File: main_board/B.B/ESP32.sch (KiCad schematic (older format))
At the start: 36 parts

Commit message: konzultace_s_Kubou_01
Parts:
- removed C?: 1nf, symbol Device:C
- removed R?: 1K, Resistor_SMD:R_0402_1005Metric, symbol Device:R
- removed R? (x2): 182, Resistor_SMD:R_0402_1005Metric, symbol Device:R
- added C?: 100nf, symbol Device:C
- added LED? (x2): LED, LED_SMD:LED_0603_1608Metric, symbol B.B-eagle-import:LED
- added R? (x4): 220, symbol Device:R
- added R?: 5k1, Resistor_SMD:R_0402_1005Metric, symbol Device:R
- C?: value 1nf -> 100nf; LCSC C1523 -> C14663
- R?: value 1K -> 5k1; LCSC (none) -> C25905
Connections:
- wire segments 104 -> 109
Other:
- moved on the sheet: C?, Q?, R?

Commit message: preparation_to_drawing_PCB
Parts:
- removed C?: 100nf, symbol Device:C
- removed C?: 1nf, symbol Device:C
- removed Q?: Q_NPN_BCE, symbol Device:Q_NPN_BCE
- removed SW?: SW_DIP_x01, symbol Switch:SW_DIP_x01
- added C?: 100nf, Capacitor_SMD:C_0402_1005Metric, symbol Device:C
- added Q?: Q_NPN_BCE, Package_TO_SOT_SMD:SOT-23, symbol Device:Q_NPN_BCE
- added SW?: SW_DIP_x01, Button_Switch_SMD:SW_Push_1P1T_NO_CK_KSC6xxJ, symbol Switch:SW_DIP_x01
- C?: footprint (none) -> Capacitor_SMD:C_0402_1005Metric; LCSC C14663 -> C1525
- J?: footprint (none) -> Connector_USB:USB_C_Receptacle_Amphenol_12401610E4-2A
- Q?: poznamka nutno vyměnit (musí být -> Vgs-min>1.6V) -> (none)
- Q?: footprint (none) -> Package_TO_SOT_SMD:SOT-23; LCSC (none) -> C125315
- R?: LCSC (none) -> C11702
- SW?: footprint (none) -> Button_Switch_SMD:SW_Push_1P1T_NO_CK_KSC6xxJ
- U?: LCSC (none) -> C105167
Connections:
- net labels added: 5V_USB
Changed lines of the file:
@@
 F 0 "J?" H 2257 3417 50  0000 C CNN
 F 1 "USB_C_Receptacle_USB2.0" H 2257 3326 50  0000 C CNN
-F 2 "" H 2300 2550 50  0001 C CNN
+F 2 "Connector_USB:USB_C_Receptacle_Amphenol_12401610E4-2A" H 2300 2550 50  0001 C CNN
 F 3 "https://www.usb.org/sites/default/files/documents/usb_type-c.zip" H 2300 2550 50  0001 C CNN
 	1    2150 2550
@@
 F 3 "https://datasheet.lcsc.com/szlcsc/Changjiang-Electronics-Tech-CJ-CJ3134K_C110100.pdf" H 3250 1350 50  0001 L CNN
 F 4 "C110100" H 3250 1350 50  0001 C CNN "LCSC"
-F 5 "nutno vyměnit (musí být ->  Vgs-min>1.6V)" H 3250 1350 50  0001 C CNN "poznamka"
 	1    3250 1350
 	0    -1   -1   0
@@
 	3300 2150 2750 2150
 Wire Wire Line
-	2750 1950 3250 1950
+	2750 1950 3050 1950
 Connection ~ 3600 1950
 $Comp
@@
 F 0 "SW?" H 9550 1667 50  0000 C CNN
 F 1 "SW_DIP_x01" H 9550 1576 50  0000 C CNN
-F 2 "" H 9550 1400 50  0001 C CNN
+F 2 "Button_Switch_SMD:SW_Push_1P1T_NO_CK_KSC6xxJ" H 9550 1400 50  0001 C CNN
 F 3 "~" H 9550 1400 50  0001 C CNN
 	1    9550 1400
@@
 Connection ~ 9900 1400
 $Comp
-L Switch:SW_DIP_x01 SW?
-U 1 1 5F936AB7
-P 9550 2400
-F 0 "SW?" H 9550 2667 50  0000 C CNN
-F 1 "SW_DIP_x01" H 9550 2576 50  0000 C CNN
-F 2 "" H 9550 2400 50  0001 C CNN
-F 3 "~" H 9550 2400 50  0001 C CNN
-	1    9550 2400
-	1    0    0    -1
-$EndComp
-$Comp
-L Device:C C?
-U 1 1 5F936ABE
-P 9550 2650
-F 0 "C?" V 9600 2750 50  0000 C CNN
-F 1 "100nf" V 9600 2500 50  0000 C CNN
-F 2 "" H 9588 2500 50  0001 C CNN
-F 3 "~" H 9550 2650 50  0001 C CNN
-F 4 "C14663" V 9550 2650 50  0001 C CNN "LCSC"
-	1    9550 2650
-	0    -1   -1   0
-$EndComp
-$Comp
 L Device:R R?
 U 1 1 5F936AC5
@@
 Connection ~ 9900 2400
 Wire Wire Line
-	10250 2400 10300 2400
-Wire Wire Line
 	10250 1400 10400 1400
 Text Label 10400 1400 0    50   ~ 0
@@
 Text Label 10400 2400 0    50   ~ 0
 EN
-$Comp
-L Device:C C?
-U 1 1 5F943646
-P 10300 2650
-F 0 "C?" V 10350 2750 50  0000 C CNN
-F 1 "1nf" V 10350 2550 50  0000 C CNN
-F 2 "" H 10338 2500 50  0001 C CNN
-F 3 "~" H 10300 2650 50  0001 C CNN
-F 4 "C1523" V 10300 2650 50  0001 C CNN "LCSC"
-	1    10300 2650
-	1    0    0    -1
-$EndComp
-Wire Wire Line
-	10300 2500 10300 2400
-$Comp
-L B.B-eagle-import:GND #GND?
-U 1 1 5F95FE63
-P 10300 2900
-F 0 "#GND?" H 10300 2900 50  0001 C CNN
-F 1 "GND" H 10300 2779 59  0000 C CNN
-F 2 "" H 10300 2900 50  0001 C CNN
-F 3 "" H 10300 2900 50  0001 C CNN
-	1    10300 2900
-	1    0    0    -1
-$EndComp
 Wire Wire Line
 	3600 1950 3900 1950
@@
 F 2 "Package_DFN_QFN:QFN-28-1EP_5x5mm_P0.5mm_EP3.35x3.35mm" H 5750 1450 50  0001 L CNN
 F 3 "https://www.silabs.com/documents/public/data-sheets/cp2102n-datasheet.pdf" H 5350 1900 50  0001 C CNN
+F 4 "C105167" H 5300 2650 50  0001 C CNN "LCSC"
 	1    5300 2650
 	1    0    0    -1
@@
 F 2 "Resistor_SMD:R_0402_1005Metric" V 4630 1450 50  0001 C CNN
 F 3 "~" H 4700 1450 50  0001 C CNN
+F 4 "C11702" H 4700 1450 50  0001 C CNN "LCSC"
 	1    4700 1450
 	1    0    0    -1
@@
 F 0 "Q?" H 8391 1646 50  0000 L CNN
 F 1 "Q_NPN_BCE" H 8391 1555 50  0000 L CNN
-F 2 "" H 8400 1700 50  0001 C CNN
+F 2 "Package_TO_SOT_SMD:SOT-23" H 8400 1700 50  0001 C CNN
 F 3 "~" H 8200 1600 50  0001 C CNN
+F 4 "C125315" H 8200 1600 50  0001 C CNN "LCSC"
 	1    8200 1600
 	1    0    0    -1
-$EndComp
-$Comp
-L Device:Q_NPN_BCE Q?
-U 1 1 5F9ABB28
-P 8200 2250
-F 0 "Q?" H 8391 2204 50  0000 L CNN
-F 1 "Q_NPN_BCE" H 8391 2295 50  0000 L CNN
-F 2 "" H 8400 2350 50  0001 C CNN
-F 3 "~" H 8200 2250 50  0001 C CNN
-	1    8200 2250
-	1    0    0    1
 $EndComp
 $Comp
@@
 F 0 "C?" V 9600 1750 50  0000 C CNN
 F 1 "100nf" V 9600 1500 50  0000 C CNN
-F 2 "" H 9588 1500 50  0001 C CNN
+F 2 "Capacitor_SMD:C_0402_1005Metric" H 9588 1500 50  0001 C CNN
 F 3 "~" H 9550 1650 50  0001 C CNN
-F 4 "C14663" V 9550 1650 50  0001 C CNN "LCSC"
+F 4 "C1525" V 9550 1650 50  0001 C CNN "LCSC"
 	1    9550 1650
 	0    -1   -1   0
 $EndComp
-Connection ~ 10300 2400
-Wire Wire Line
-	10300 2400 10400 2400
 $Comp
 L Device:R R?
@@
 	-1   0    0    1
 $EndComp
+Text HLabel 3050 1850 1    50   Input ~ 0
+5V_USB
+Wire Wire Line
+	3050 1850 3050 1950
+Connection ~ 3050 1950
+Wire Wire Line
+	3050 1950 3250 1950
+$Comp
+L Device:Q_NPN_BCE Q?
+U 1 1 5FB13B7B
+P 8200 2250
+F 0 "Q?" H 8391 2296 50  0000 L CNN
+F 1 "Q_NPN_BCE" H 8391 2205 50  0000 L CNN
+F 2 "Package_TO_SOT_SMD:SOT-23" H 8400 2350 50  0001 C CNN
+F 3 "~" H 8200 2250 50  0001 C CNN
+F 4 "C125315" H 8200 2250 50  0001 C CNN "LCSC"
+	1    8200 2250
+	1    0    0    1
+$EndComp
+$Comp
+L Switch:SW_DIP_x01 SW?
+U 1 1 5FB1B20F
+P 9550 2400
+F 0 "SW?" H 9550 2667 50  0000 C CNN
+F 1 "SW_DIP_x01" H 9550 2576 50  0000 C CNN
+F 2 "Button_Switch_SMD:SW_Push_1P1T_NO_CK_KSC6xxJ" H 9550 2400 50  0001 C CNN
+F 3 "~" H 9550 2400 50  0001 C CNN
+	1    9550 2400
+	1    0    0    -1
+$EndComp
+$Comp
+L Device:C C?
+U 1 1 5FB1BF0E
+P 9550 2650
+F 0 "C?" V 9600 2750 50  0000 C CNN
+F 1 "100nf" V 9600 2500 50  0000 C CNN
+F 2 "Capacitor_SMD:C_0402_1005Metric" H 9588 2500 50  0001 C CNN
+F 3 "~" H 9550 2650 50  0001 C CNN
+F 4 "C1525" V 9550 2650 50  0001 C CNN "LCSC"
+	1    9550 2650
+	0    -1   -1   0
+$EndComp
+Wire Wire Line
+	10250 2400 10400 2400
 $EndSCHEMATC

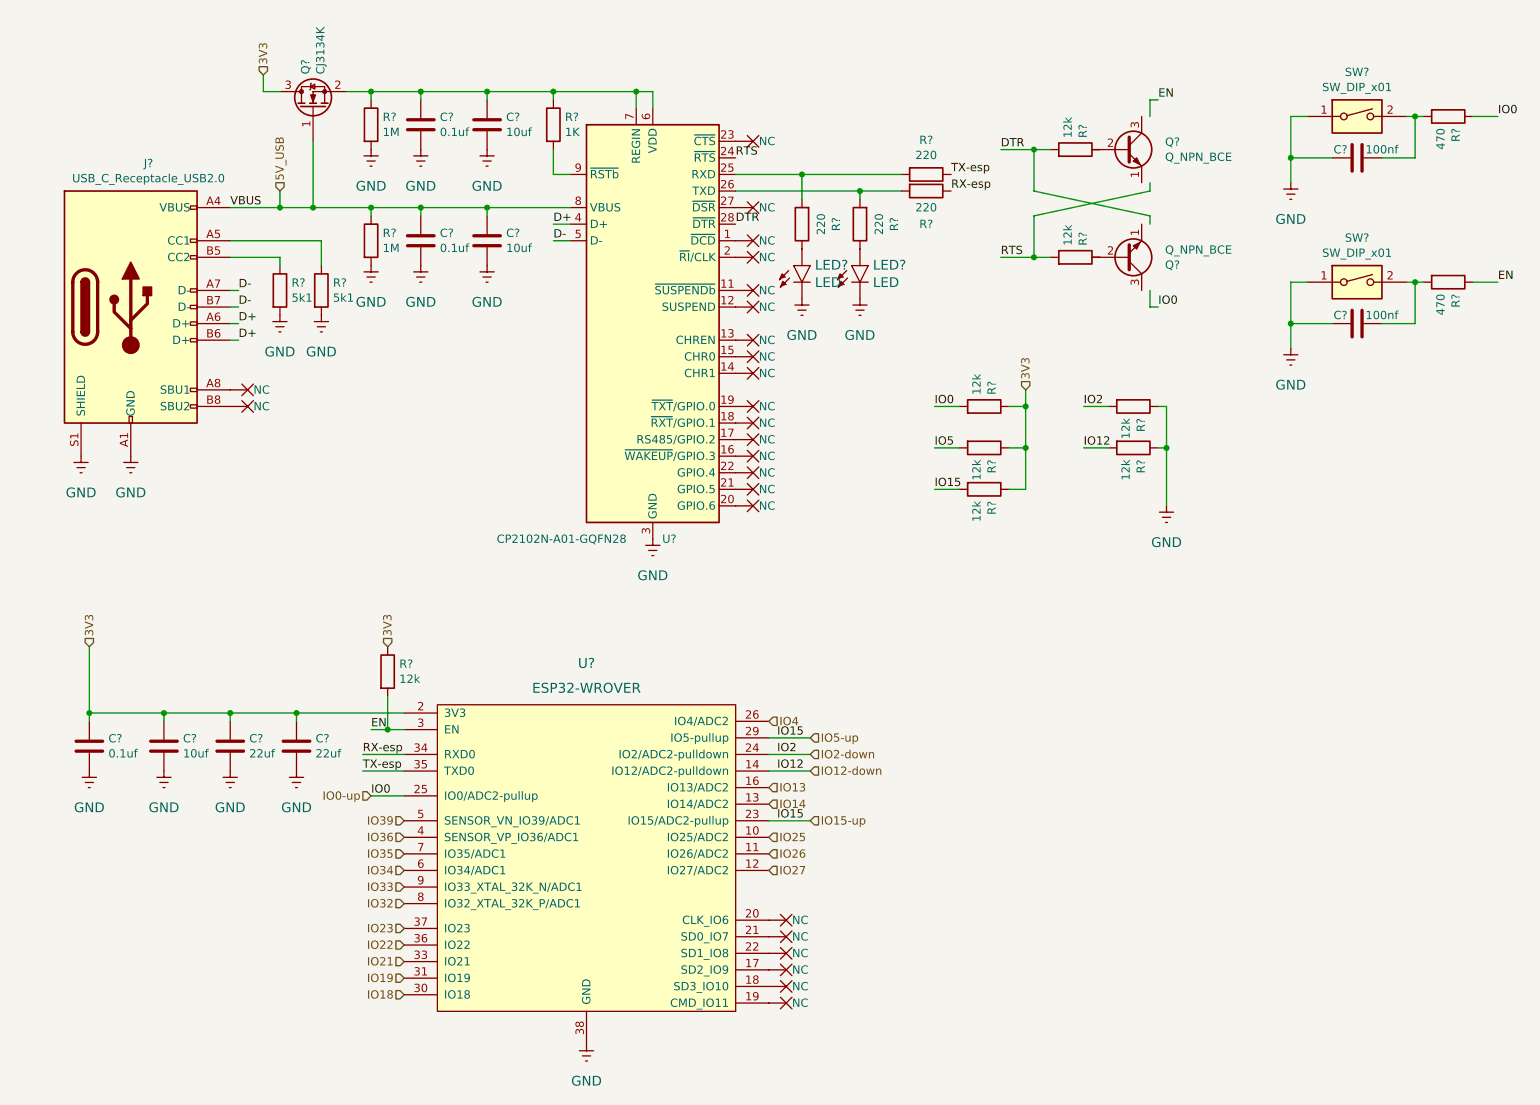
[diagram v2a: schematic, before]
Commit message: complete_preparation_to_drawing_PCB
footprint for all component and LCSC code for everything for mounting in JLCPCB
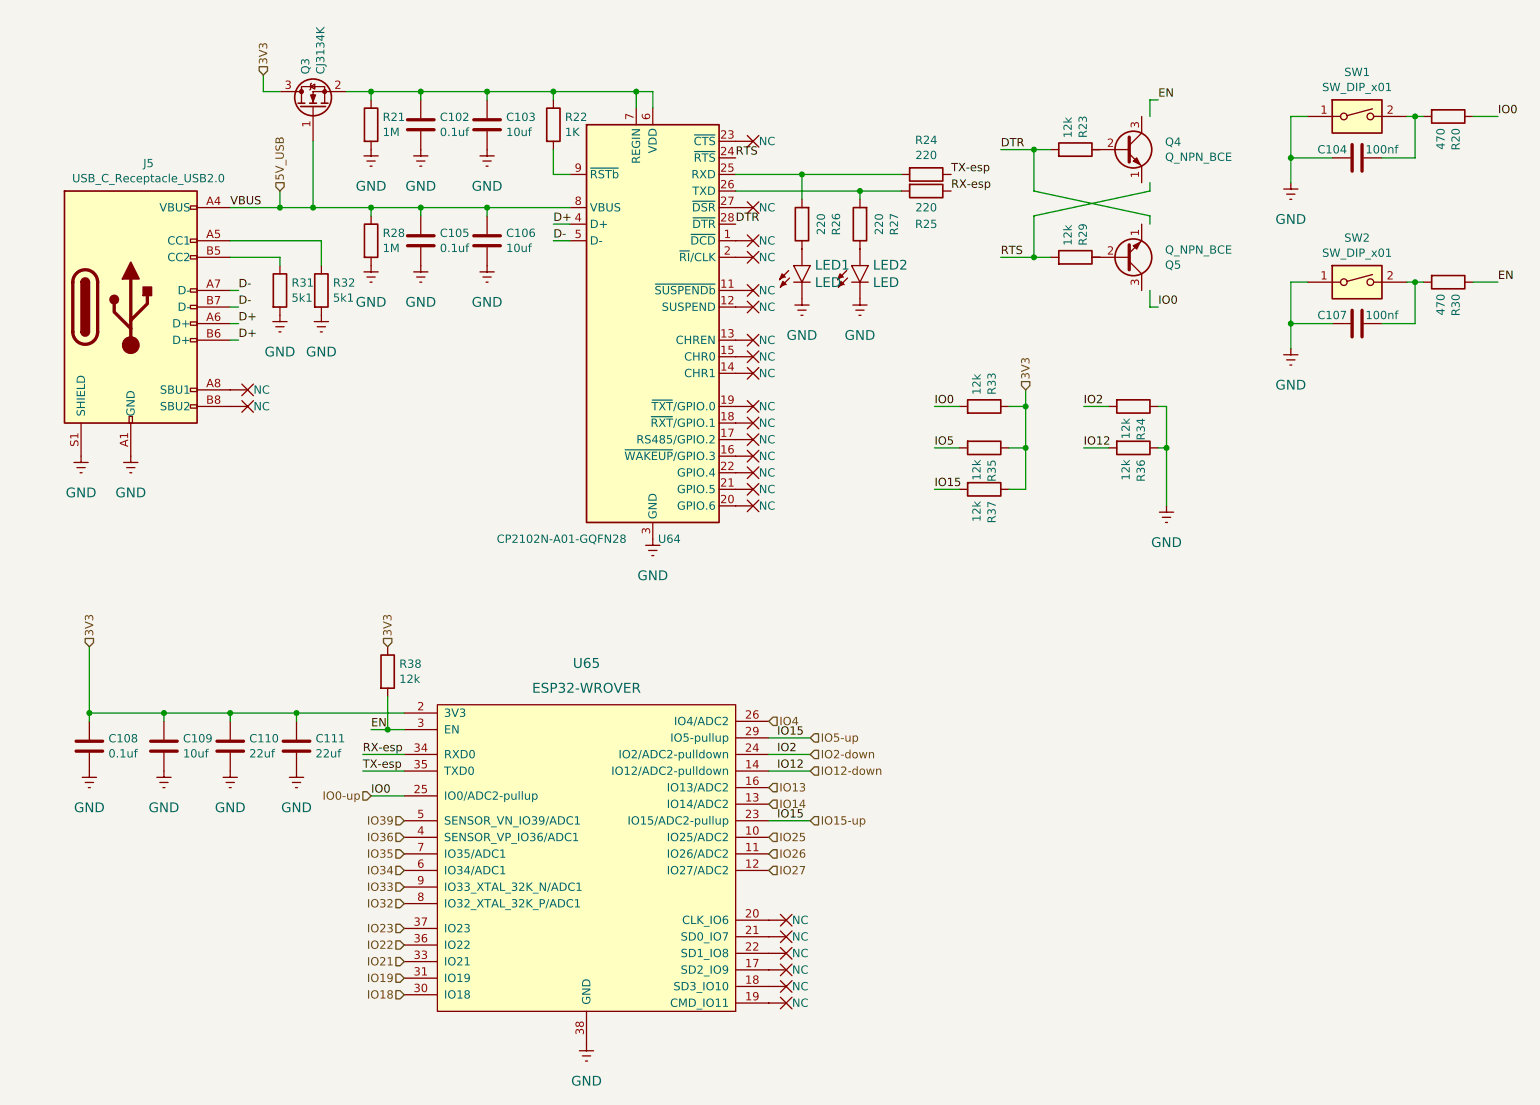
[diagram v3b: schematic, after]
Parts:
- removed R?: 12k, symbol Device:R
- added R38: 12k, Resistor_SMD:R_0402_1005Metric, symbol Device:R
- R24, R25, R26, R27: renamed from R?; footprint (none) -> Resistor_SMD:R_0402_1005Metric
- SW1, SW2: renamed from SW?; LCSC (none) -> C318889
- gave numbers to parts that had none: 32

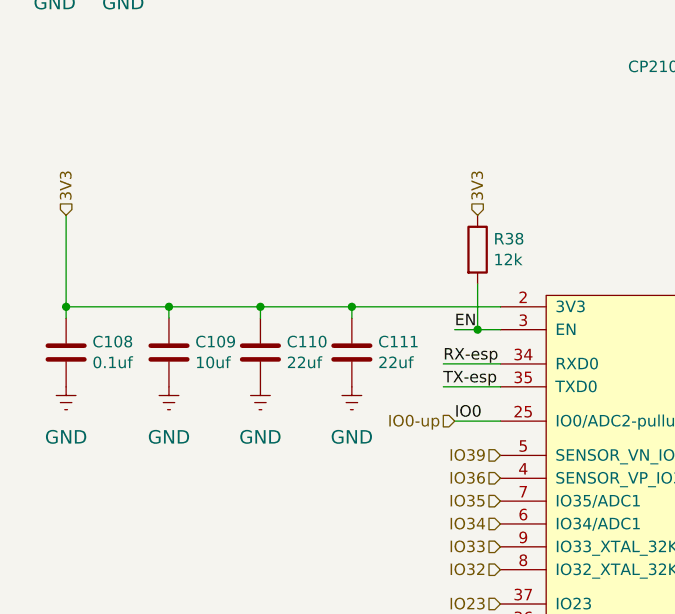
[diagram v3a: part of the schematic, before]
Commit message: optimalizace_kondenzatoru
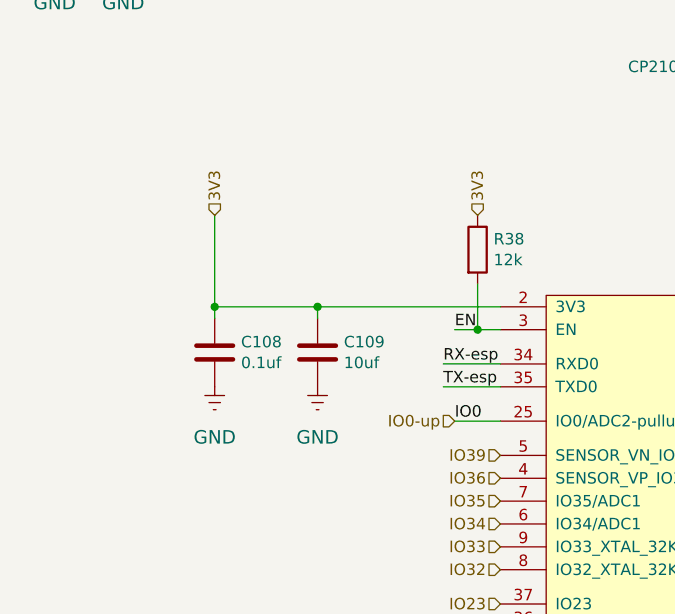
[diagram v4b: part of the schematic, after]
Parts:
- removed C110, C111: 22uf, Capacitor_SMD:C_0805_2012Metric, symbol Device:C
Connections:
- wire segments 109 -> 105
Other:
- moved on the sheet: C108, C109
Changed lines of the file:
@@
 	2950 1250 2950 1150
 Wire Wire Line
-	1900 4600 1900 5000
-Wire Wire Line
-	1900 5000 2350 5000
+	2550 4600 2550 5000
+Wire Wire Line
+	2550 5000 3000 5000
 Wire Wire Line
 	8300 2450 8300 2550
@@
 Wire Wire Line
 	3900 1950 4300 1950
-$Comp
-L Device:C C111
-U 1 1 5F8F8C8C
-P 3150 5200
-F 0 "C111" H 3265 5246 50  0000 L CNN
-F 1 "22uf" H 3265 5155 50  0000 L CNN
-F 2 "Capacitor_SMD:C_0805_2012Metric" H 3188 5050 50  0001 C CNN
-F 3 "https://datasheet.lcsc.com/szlcsc/Samsung-Electro-Mechanics-CL21A226MAQNNNE_C45783.pdf" H 3150 5200 50  0001 C CNN
-F 4 "C45783" H 3150 5200 50  0001 C CNN "LCSC"
-	1    3150 5200
-	1    0    0    -1
-$EndComp
-Wire Wire Line
-	3150 5050 3150 5000
-Connection ~ 3150 5000
-Wire Wire Line
-	3150 5000 3800 5000
-Connection ~ 2750 5000
-Wire Wire Line
-	2750 5000 3150 5000
-Wire Wire Line
-	2350 5050 2350 5000
-Connection ~ 2350 5000
-Wire Wire Line
-	2350 5000 2750 5000
-Wire Wire Line
-	1900 5050 1900 5000
-Connection ~ 1900 5000
-Wire Wire Line
-	2750 5050 2750 5000
-$Comp
-L Device:C C110
-U 1 1 5F8FB2CD
-P 2750 5200
-F 0 "C110" H 2865 5246 50  0000 L CNN
-F 1 "22uf" H 2865 5155 50  0000 L CNN
-F 2 "Capacitor_SMD:C_0805_2012Metric" H 2788 5050 50  0001 C CNN
-F 3 "https://datasheet.lcsc.com/szlcsc/Samsung-Electro-Mechanics-CL21A226MAQNNNE_C45783.pdf" H 2750 5200 50  0001 C CNN
-F 4 "C45783" H 2750 5200 50  0001 C CNN "LCSC"
-	1    2750 5200
-	1    0    0    -1
-$EndComp
-$Comp
-L B.B-eagle-import:GND #GND0128
-U 1 1 5F96D25A
-P 3150 5450
-F 0 "#GND0128" H 3150 5450 50  0001 C CNN
-F 1 "GND" H 3150 5329 59  0000 C CNN
-F 2 "" H 3150 5450 50  0001 C CNN
-F 3 "" H 3150 5450 50  0001 C CNN
-	1    3150 5450
-	1    0    0    -1
-$EndComp
-$Comp
-L B.B-eagle-import:GND #GND0127
-U 1 1 5F96D6D1
-P 2750 5450
-F 0 "#GND0127" H 2750 5450 50  0001 C CNN
-F 1 "GND" H 2750 5329 59  0000 C CNN
-F 2 "" H 2750 5450 50  0001 C CNN
-F 3 "" H 2750 5450 50  0001 C CNN
-	1    2750 5450
-	1    0    0    -1
-$EndComp
+Wire Wire Line
+	3000 5050 3000 5000
+Wire Wire Line
+	2550 5050 2550 5000
+Connection ~ 2550 5000
 $Comp
 L B.B-eagle-import:GND #GND0126
 U 1 1 5F96DA82
-P 2350 5450
-F 0 "#GND0126" H 2350 5450 50  0001 C CNN
-F 1 "GND" H 2350 5329 59  0000 C CNN
-F 2 "" H 2350 5450 50  0001 C CNN
-F 3 "" H 2350 5450 50  0001 C CNN
-	1    2350 5450
+P 3000 5450
+F 0 "#GND0126" H 3000 5450 50  0001 C CNN
+F 1 "GND" H 3000 5329 59  0000 C CNN
+F 2 "" H 3000 5450 50  0001 C CNN
+F 3 "" H 3000 5450 50  0001 C CNN
+	1    3000 5450
 	1    0    0    -1
 $EndComp
@@
 L B.B-eagle-import:GND #GND0125
 U 1 1 5F96DE9E
-P 1900 5450
-F 0 "#GND0125" H 1900 5450 50  0001 C CNN
-F 1 "GND" H 1900 5329 59  0000 C CNN
-F 2 "" H 1900 5450 50  0001 C CNN
-F 3 "" H 1900 5450 50  0001 C CNN
-	1    1900 5450
+P 2550 5450
+F 0 "#GND0125" H 2550 5450 50  0001 C CNN
+F 1 "GND" H 2550 5329 59  0000 C CNN
+F 2 "" H 2550 5450 50  0001 C CNN
+F 3 "" H 2550 5450 50  0001 C CNN
+	1    2550 5450
 	1    0    0    -1
 $EndComp
@@
 L Device:C C109
 U 1 1 5F970DFC
-P 2350 5200
-F 0 "C109" H 2465 5246 50  0000 L CNN
-F 1 "10uf" H 2465 5155 50  0000 L CNN
-F 2 "Capacitor_SMD:C_0805_2012Metric" H 2388 5050 50  0001 C CNN
-F 3 "~" H 2350 5200 50  0001 C CNN
-F 4 "C15850" H 2350 5200 50  0001 C CNN "LCSC"
-	1    2350 5200
+P 3000 5200
+F 0 "C109" H 3115 5246 50  0000 L CNN
+F 1 "10uf" H 3115 5155 50  0000 L CNN
+F 2 "Capacitor_SMD:C_0805_2012Metric" H 3038 5050 50  0001 C CNN
+F 3 "~" H 3000 5200 50  0001 C CNN
+F 4 "C15850" H 3000 5200 50  0001 C CNN "LCSC"
+	1    3000 5200
 	1    0    0    -1
 $EndComp
@@
 L Device:C C108
 U 1 1 5F971517
-P 1900 5200
-F 0 "C108" H 2015 5246 50  0000 L CNN
-F 1 "0.1uf" H 2015 5155 50  0000 L CNN
-F 2 "Capacitor_SMD:C_0805_2012Metric" H 1938 5050 50  0001 C CNN
-F 3 "~" H 1900 5200 50  0001 C CNN
-F 4 "C14663" H 1900 5200 50  0001 C CNN "LCSC"
-	1    1900 5200
+P 2550 5200
+F 0 "C108" H 2665 5246 50  0000 L CNN
+F 1 "0.1uf" H 2665 5155 50  0000 L CNN
+F 2 "Capacitor_SMD:C_0805_2012Metric" H 2588 5050 50  0001 C CNN
+F 3 "~" H 2550 5200 50  0001 C CNN
+F 4 "C14663" H 2550 5200 50  0001 C CNN "LCSC"
+	1    2550 5200
 	1    0    0    -1
 $EndComp
@@
 Wire Wire Line
 	6800 1850 6550 1850
-Text HLabel 1900 4600 1    50   Input ~ 0
+Text HLabel 2550 4600 1    50   Input ~ 0
 3V3
 Text HLabel 3700 4600 1    50   Input ~ 0
@@
 	1    0    0    -1
 $EndComp
+Wire Wire Line
+	3000 5000 3800 5000
+Connection ~ 3000 5000
 $EndSCHEMATC

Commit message: start vith pcb
firsxxt proposal component layout of main board
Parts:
- U65: footprint esp32-wrover:ESP32-WROVER -> BB:ESP32-WROVER
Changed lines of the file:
@@
 EESchema Schematic File Version 4
-LIBS:B.B-cache
-EELAYER 29 0
+EELAYER 30 0
 EELAYER END
 $Descr A4 11693 8268
@@
 F 0 "U65" H 4900 6900 60  0000 C CNN
 F 1 "ESP32-WROVER" H 4900 6750 60  0000 C CNN
-F 2 "esp32-wrover:ESP32-WROVER" H 5350 5500 60  0001 C CNN
+F 2 "BB:ESP32-WROVER" H 5350 5500 60  0001 C CNN
 F 3 "" H 5350 5500 60  0001 C CNN
 	1    4900 5800
@@
 IO0
 Text Label 6050 5150 0    50   ~ 0
-IO15
+IO5
 Text Label 6050 5250 0    50   ~ 0
 IO2
